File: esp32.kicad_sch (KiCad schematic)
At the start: 31 parts, among them J2 TC2030-IDC, J3 Conn_01x04, J4 USB_C_Receptacle_USB2.0, SW1 TL3330AF260QG, SW2 TL3330AF260QG, U7 RT9080-33GJ5, U8 ESP32-S3-WROOM-1, Y2 32.768kHz

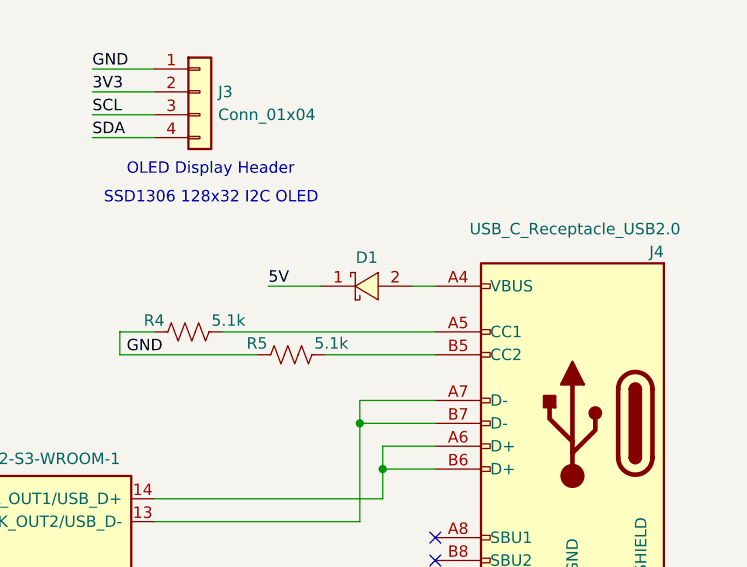
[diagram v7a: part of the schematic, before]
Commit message: switched barrel plug for #8. touched up schematic, DRC, generated BOM, generated Gerbers
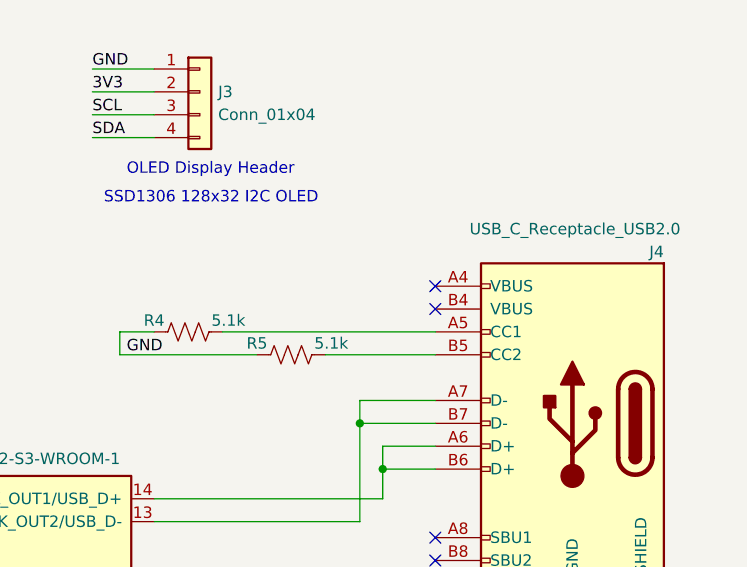
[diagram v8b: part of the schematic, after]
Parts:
- removed D1: SS310, Diode_SMD:D_SMA, symbol lcsc:SS310_C85658
- J2: now left out of the parts list
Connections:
- net at J4.A4 (VBUS), J4.A9 (VBUS): no longer J4.B4 (VBUS), J4.B9 (VBUS)
- new net: J4.B4 (VBUS), J4.B9 (VBUS)
- no-connect marks 22 -> 24
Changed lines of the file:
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@@
   (title_block
     (title "blockaxe1")
-    (date "2023-11-15")
-    (rev "1")
+    (date "2024-02-21")
+    (rev "2")
   )
   (junction (at 132.842 27.94) (diameter 0) (color 0 0 0 0)
@@
   (no_connect (at 86.36 103.632))
   (no_connect (at 86.36 90.932))
+  (no_connect (at 231.902 54.61))
   (no_connect (at 200.66 111.252))
   (no_connect (at 86.36 98.552))
@@
   (no_connect (at 200.66 123.952))
   (no_connect (at 200.66 116.332))
+  (no_connect (at 231.902 52.07))
   (no_connect (at 200.66 96.012))
   (no_connect (at 200.66 90.932))
@@
     (stroke (width 0) (type default))
   )
-  (wire (pts (xy 213.36 52.07) (xy 219.202 52.07))
-    (stroke (width 0) (type default))
-  )
   (wire (pts (xy 44.45 78.232) (xy 86.36 78.232))
     (stroke (width 0) (type default))
@@
   )
   (wire (pts (xy 226.06 72.39) (xy 226.06 69.85))
-    (stroke (width 0) (type default))
-  )
-  (wire (pts (xy 229.362 52.07) (xy 231.902 52.07))
     (stroke (width 0) (type default))
   )
@@
   )
   (label "3V3" (at 75.692 134.112 0) (fields_autoplaced)
-    (effects (font (size 1.27 1.27)) (justify left bottom))
-  )
-  (label "5V" (at 213.36 52.07 0) (fields_autoplaced)
     (effects (font (size 1.27 1.27)) (justify left bottom))
   )
@@
       (effects (font (size 1.27 1.27)) hide)
     )
-    (property "Datasheet" "https://gct.co/connector/usb4105" (at 243.332 67.31 0)
+    (property "Datasheet" "https://www.usb.org/sites/default/files/documents/usb_type-c.zip" (at 243.332 67.31 0)
       (effects (font (size 1.27 1.27)) hide)
     )
@@
   )
   (symbol (lib_id "blockaxe:TC2030-IDC-NL") (at 74.93 166.37 0) (unit 1)
-    (in_bom yes) (on_board yes) (dnp no) (fields_autoplaced)
+    (in_bom no) (on_board yes) (dnp no) (fields_autoplaced)
     (property "Reference" "J2" (at 74.93 153.67 0)
       (effects (font (size 1.27 1.27)))
@@
         )
       )
-    )
-  )
-  (symbol (lib_id "lcsc:SS310_C85658") (at 224.282 52.07 0) (unit 1)
-    (in_bom yes) (on_board yes) (dnp no)
-    (property "Reference" "D1" (at 224.282 48.895 0)
-      (effects (font (size 1.27 1.27)))
-    )
-    (property "Value" "SS310" (at 225.552 57.15 0)
-      (effects (font (size 1.27 1.27)) hide)
-    )
-    (property "Footprint" "Diode_SMD:D_SMA" (at 224.282 59.69 0)
-      (effects (font (size 1.27 1.27)) hide)
-    )
-    (property "Datasheet" "https://www.mccsemi.com/pdf/Products/SK32A-L-SK310A-L(DO-214AC).pdf" (at 224.282 62.23 0)
-      (effects (font (size 1.27 1.27)) hide)
-    )
-    (property "DK" "SK310A-LTPMSCT-ND" (at 224.282 52.07 0)
-      (effects (font (size 1.27 1.27)) hide)
-    )
-    (property "PARTNO" "SK310A-LTP" (at 224.282 52.07 0)
-      (effects (font (size 1.27 1.27)) hide)
-    )
-    (pin "1")
-    (pin "2")
-    (instances
-      (project "blockaxe1"
-        (path "/a166cb37-4e3a-4be5-b2da-277a3281a4de/97fce8a4-b016-4d76-8490-b8c988e88337"
-          (reference "D1") (unit 1)
-        )
-      )
-      (project "esp32"
-        (path "/dcd2fc1c-da48-40a9-b97c-5712d9530f4f"
-          (reference "D1") (unit 1)
-        )
-      )
-      (project "bitaxeUltra"
-        (path "/e63e39d7-6ac0-4ffd-8aa3-1841a4541b55/ca857324-2ec8-447e-bd58-90d0c2e6b6d7"
-          (reference "D1") (unit 1)
-        )
-      )
